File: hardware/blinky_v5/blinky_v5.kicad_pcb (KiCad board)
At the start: 2 copper layers, 130 x 70 mm, 237 parts, among them J1 RJ45, J10 Conn_01x04, J11 Conn_01x08, J12 Conn_01x06, J2 Conn_01x06_Pin, J3 Conn_01x05_Pin, J5 Conn_01x06_Pin, J6 Conn_01x04_Pin, J7 Conn_01x04_Pin, J8 Conn_01x02, J9 Conn_02x10_Odd_Even, Q1 2N7002, Q2 2N7002, Q3 2N7002, Q4 2N7002, Q5 2N7002, Q6 2N7002, Q7 2N7002, Q8 2N7002, U1 ADA4807-1, U10 STM32F405RGTx, U11 AMS1117-3.3, U12 BA50DD0WHFP-TR, U13 M24C02-RMN, U2 SN74LVC1G14DBV, U3 SN74LVC1G14DBV, U4 ADA4807-1, U5 ADA4807-1, U6 TLV3603DCKR, U7 SN74LVC1G14DBV, U8 TLV3603DCKR, U9 L78L05_SOT89, X1 GTXO-14V (2.048MHz), X2 GTXO-14V (2.048MHz), Y1 AOCJY4A-10.000MHZ-SW, Y2 16MHz

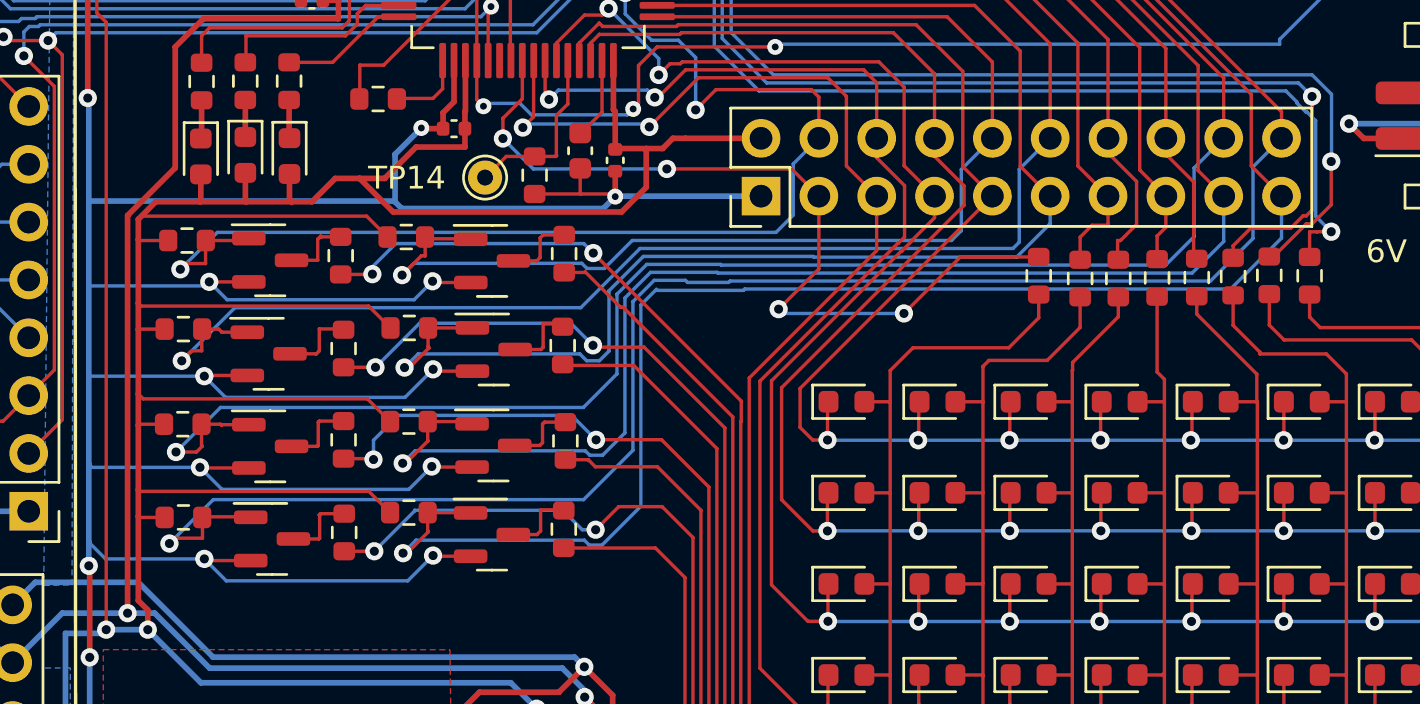
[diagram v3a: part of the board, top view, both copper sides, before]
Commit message: move LED resistors to pull down from pull up
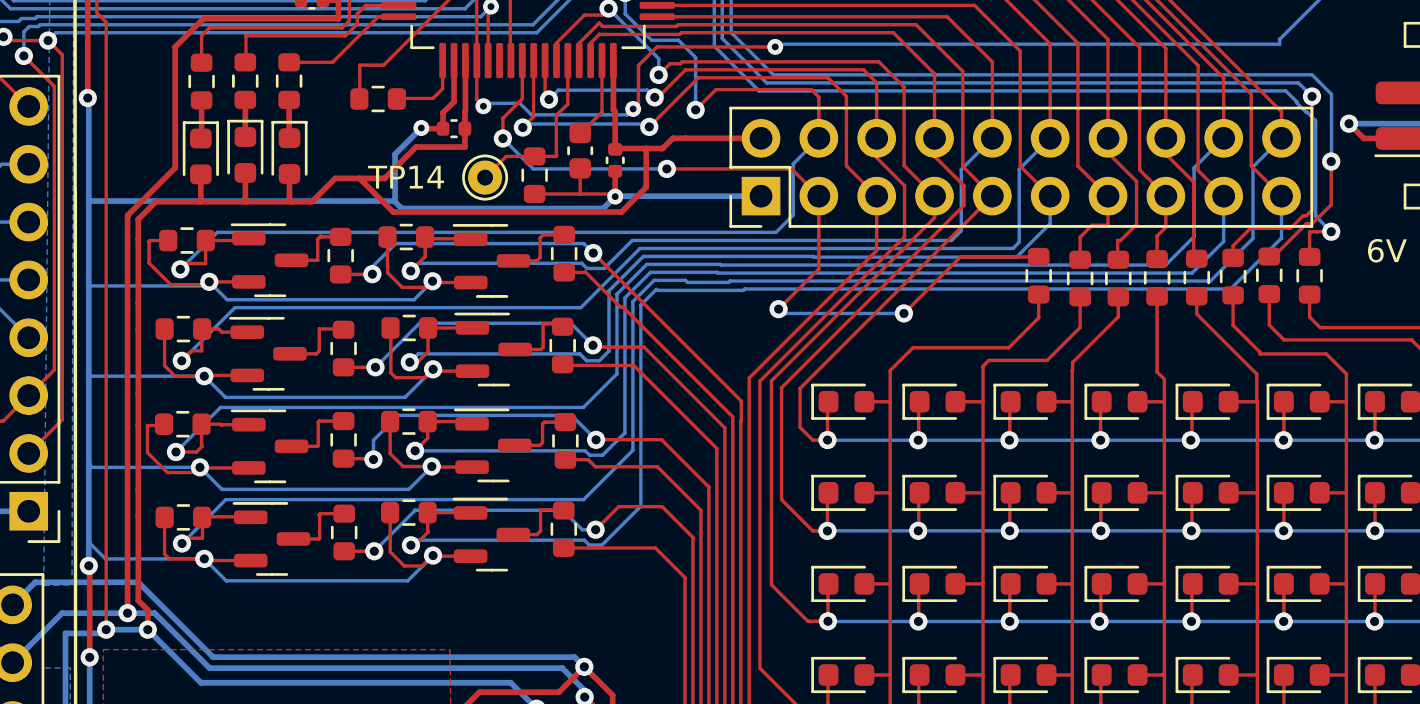
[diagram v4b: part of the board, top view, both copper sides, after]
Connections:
- R33 pad 1: +3.3V -> GND
- R35 pad 1: +3.3V -> GND
- R37 pad 1: +3.3V -> GND
- R39 pad 1: +3.3V -> GND
- R41 pad 1: +3.3V -> GND
- R43 pad 1: +3.3V -> GND
- R45 pad 1: +3.3V -> GND
- R47 pad 1: +3.3V -> GND
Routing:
- net +3.3V: track 468.5 -> 417.8 mm
- net GND: track 1175.8 -> 1207.8 mm
- net /LEDE: track 83.1 -> 81.5 mm
- net /LEDB: track 99.4 -> 98.3 mm
- net /LEDC: track 90.6 -> 89.7 mm
- net /LEDH: track 53.3 -> 52.4 mm
- net /LEDG: track 62.0 -> 61.4 mm

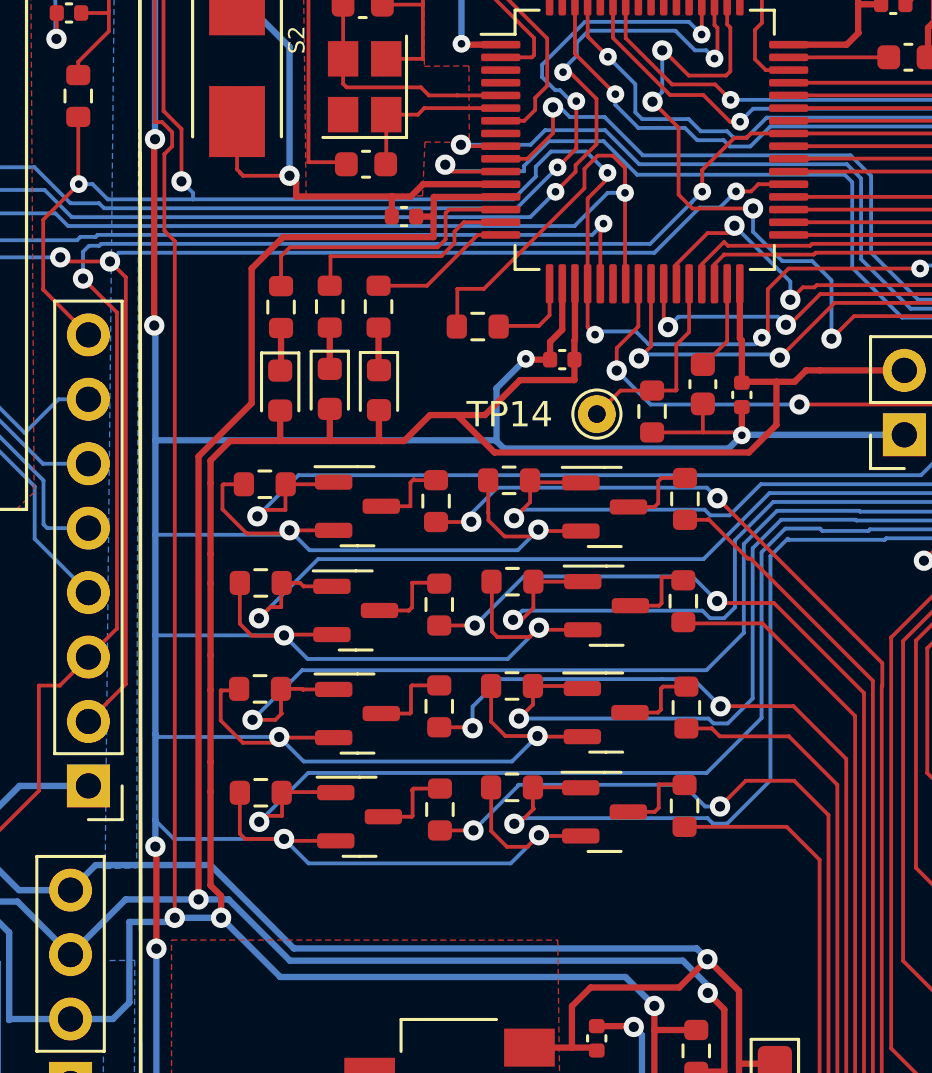
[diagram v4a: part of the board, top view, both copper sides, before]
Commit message: update to have FET drivers for some of status LEDs
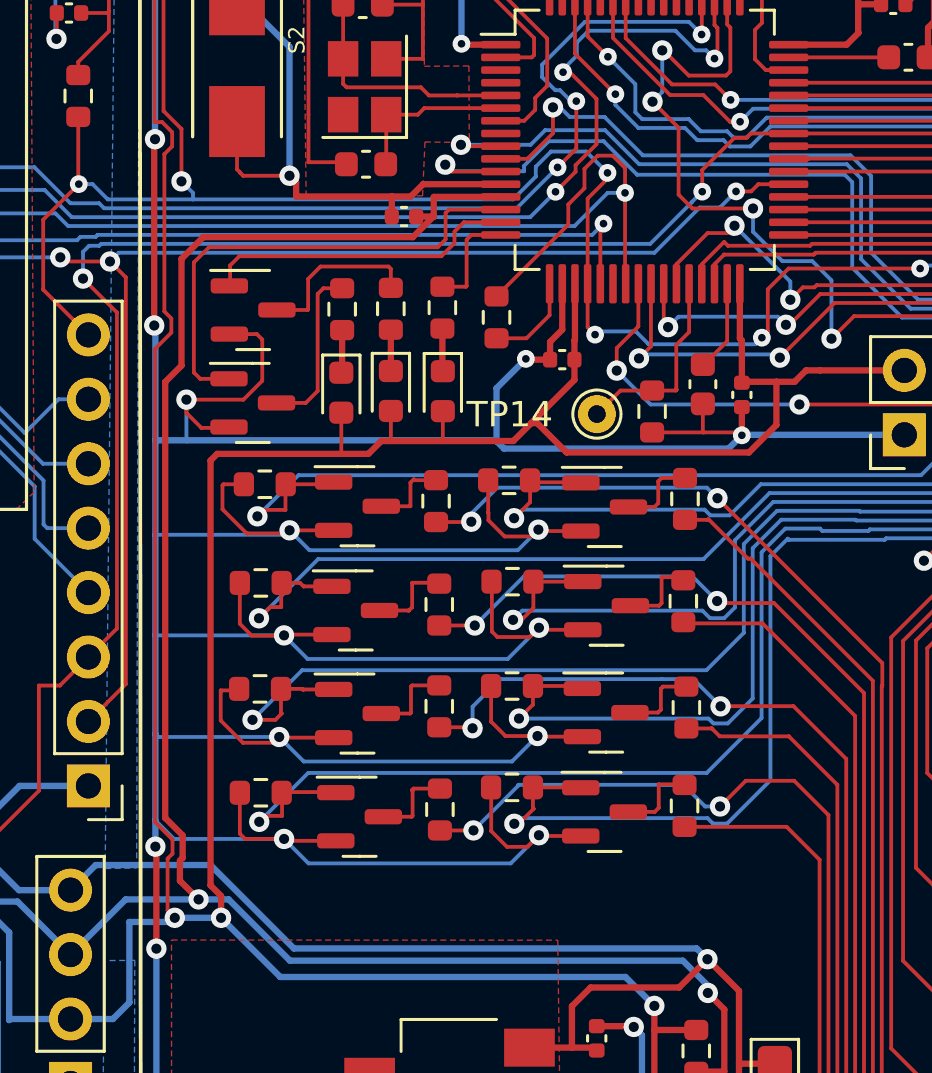
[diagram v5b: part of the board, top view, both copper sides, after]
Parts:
- added Q10: 2N7002, Package_TO_SOT_SMD:SOT-23, F.Cu at (167.6, 81.7)
- added Q9: 2N7002, Package_TO_SOT_SMD:SOT-23, F.Cu at (167.6, 78.0)
- moved D1 2.52 mm to (175.1, 81.2)
- moved R30 2.52 mm to (175.0, 78.0)
- moved D2 2.41 mm to (173.0, 81.2)
- moved D3 2.41 mm to (171.1, 81.3)
- moved R29 2.41 mm to (173.0, 78.0)
- moved R31 2.41 mm to (171.1, 78.0)
- moved R54 0.83 mm to (177.2, 78.3), turned to -90 degrees
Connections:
- R29 pad 2: /LEDM1 -> Net-(Q9-D)
- R31 pad 2: /LEDM3 -> Net-(Q10-D)
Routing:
- net GND: track 1207.8 -> 1218.2 mm, vias 60 -> 61
- net /LEDM3: track 11.2 -> 19.4 mm
- net Net-(Q10-D): track 0.00 -> 6.70 mm
- net Net-(Q9-D): track 0.00 -> 6.69 mm
- net /LEDM1: track 8.71 -> 12.5 mm
- net +3.3VA: track 201.7 -> 204.3 mm
- net SYNC_OUT: track 115.0 -> 112.5 mm
- net +3.3V: track 417.8 -> 415.8 mm
- net /LEDM2: track 5.65 -> 4.21 mm

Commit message: update schematic for new pin out
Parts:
- removed JP5: SolderJumper_2_Bridged, Jumper:SolderJumper-2_P1.3mm_Bridged_RoundedPad1.0x1.5mm
- removed X1: GTXO-14V (2.048MHz), Oscillator:Oscillator_DIP-14
- added J4: Conn_01x04_Pin, Connector_PinHeader_2.54mm:PinHeader_1x04_P2.54mm_Vertical, F.Cu at (235.8, 66.6)
- added R60: 1K0, Resistor_SMD:R_0603_1608Metric, F.Cu at (141.5, 125.4)
- added R61: 1K0, Resistor_SMD:R_0603_1608Metric, F.Cu at (149.4, 125.9)
- added R62: 1K0, Resistor_SMD:R_0603_1608Metric, F.Cu at (172.3, 134.5)
- added R63: 1K0, Resistor_SMD:R_0603_1608Metric, F.Cu at (161.1, 139.2)
- added R64: 1K0, Resistor_SMD:R_0603_1608Metric, F.Cu at (190.6, 136.1)
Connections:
- J11 pad 3: EXT_CLK_IN -> /CLK
- J12 pad 3: /SWDTRC -> GND
- TP10 pad 1: EXT_CLK_IN -> AUX_CLK
- TP3 pad 1: SYNC_IN -> Net-(R63-Pad2)
- TP8 pad 1: GPS_PPS -> Net-(U8-OUT)
- U10 pad 14: /LEDM3 -> AUX_CLK
- U10 pad 15: /LEDM1 -> AUX_GPS_PPS
- U10 pad 16: /LEDM2 -> /AUX_SYNC_MON
- U10 pad 17: /SYNC_MON -> /LEDM3
- U10 pad 21: SYNC_IN -> /AUD_OUT
- U10 pad 22: unconnected-(U10-PA6-Pad22) -> /COL1
- U10 pad 23: SYNC_OUT -> /COL2
- U10 pad 29: /COL2 -> GPS_PPS
- U10 pad 3: unconnected-(U10-PC14-Pad3) -> /LEDM1
- U10 pad 30: /COL1 -> /SYNC_MON
- U10 pad 37: GPS_PPS -> SYNC_IN2
- U10 pad 4: unconnected-(U10-PC15-Pad4) -> /LEDM2
- U10 pad 41: EXT_CLK_IN -> SYNC_OUT
- U10 pad 50: /LEDA -> /CLK
- U10 pad 53: /DB4 -> /LEDA
- U10 pad 55: /SWDTRC -> SYNC_IN
- U10 pad 8: unconnected-(U10-PC0-Pad8) -> /AUD_IN
- U3 pad 4: SYNC_IN -> Net-(R63-Pad2)
- U7 pad 4: Net-(JP5-A) -> AUX_CLK
- U8 pad 1: GPS_PPS -> Net-(U8-OUT)
- X2 pad 8: EXT_CLK_IN -> /CLK
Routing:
- net (no net): track 0.00 -> 152.3 mm
- net EXT_CLK_IN: track 125.3 -> 0.00 mm, vias 6 -> 0
- net GND: track 1218.2 -> 1185.7 mm, vias 61 -> 60
- net /SWDTRC: track 27.0 -> 0.00 mm, vias 2 -> 0
- net /OCXO_OUT: track 69.9 -> 63.3 mm
- net /Vadj: track 56.0 -> 49.5 mm
- net Net-(JP5-A): track 3.31 -> 0.00 mm
- net AUX_CLK: track 0.00 -> 3.31 mm
- net +3.3VA: track 204.3 -> 205.2 mm
- net SYNC_IN: vias 4 -> 6
- net /CLK: vias 0 -> 6

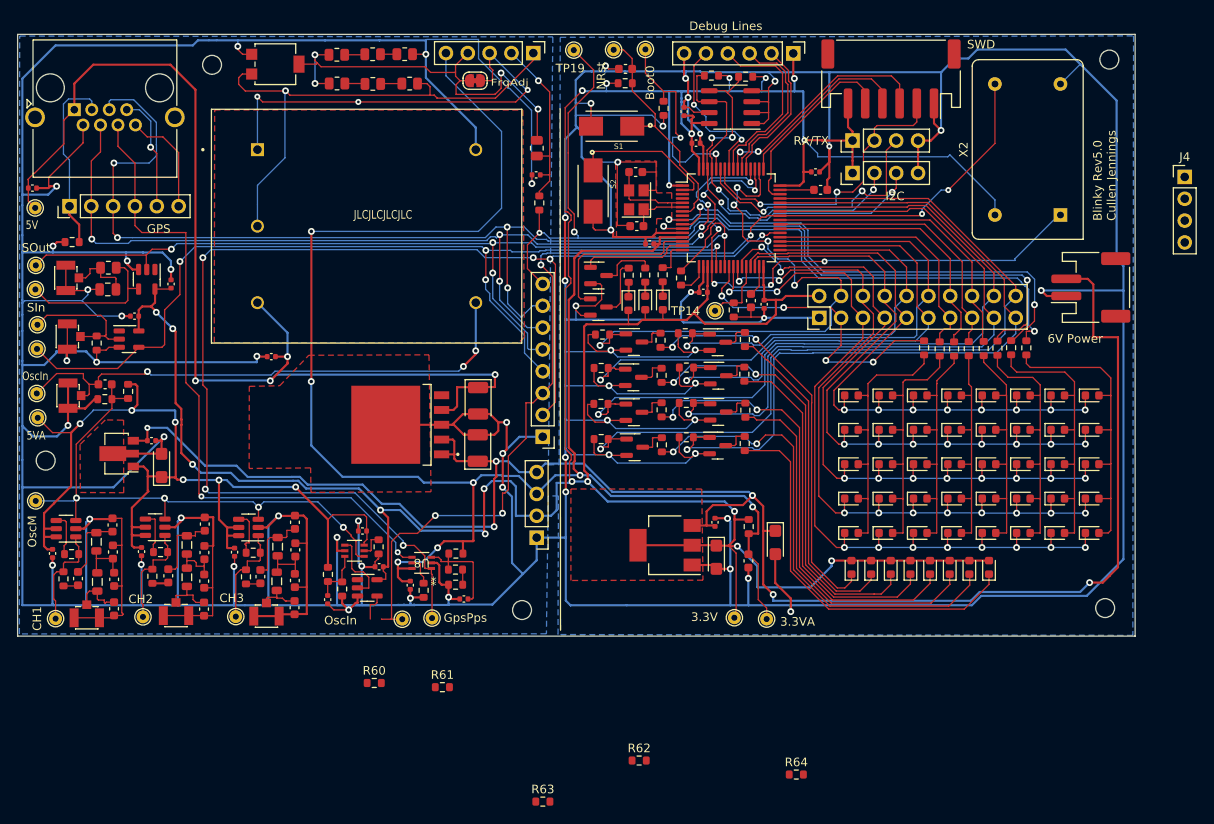
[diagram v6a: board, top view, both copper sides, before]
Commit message: update scehmatic with new pin out
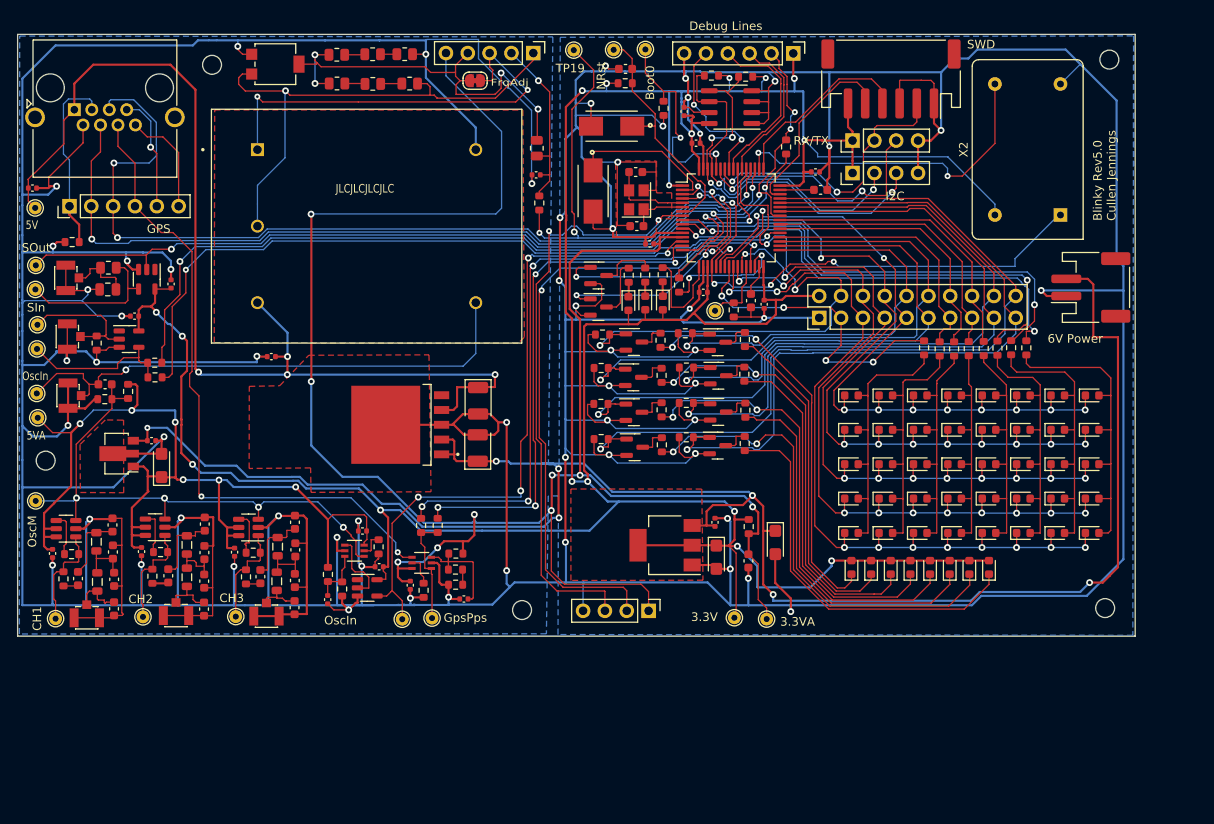
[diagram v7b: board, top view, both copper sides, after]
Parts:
- removed J10: Conn_01x04, Connector_PinHeader_2.54mm:PinHeader_1x04_P2.54mm_Vertical
- removed J11: Conn_01x08, Connector_PinHeader_2.54mm:PinHeader_1x08_P2.54mm_Vertical
- moved R64 87.7 mm to (116.0, 89.9), turned to 180 degrees
- moved J4 80.2 mm to (173.4, 117.1), turned to -90 degrees
- moved R62 73.4 mm to (189.4, 63.1), turned to -90 degrees
- moved R63 68.2 mm to (115.9, 88.2), turned to 180 degrees
- moved R60 19.1 mm to (146.9, 107.1), turned to -90 degrees
- moved R61 18.8 mm to (148.9, 107.1), turned to 90 degrees
- moved R54 0.85 mm to (176.9, 79.2)
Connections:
- J5 pad 2: /DB4 -> SYNC_OUT
- U10 pad 17: /LEDM3 -> /LEDM2
- U10 pad 3: /LEDM1 -> /LEDM3
- U10 pad 4: /LEDM2 -> /LEDM1
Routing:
- net (no net): track 152.3 -> 0.00 mm
- net SYNC_IN2: track 0.00 -> 86.2 mm, vias 0 -> 2
- net GPS_PPS: track 152.6 -> 71.2 mm, vias 6 -> 4
- net AUX_CLK: track 3.31 -> 77.2 mm, vias 0 -> 4
- net /AUD_OUT: track 0.00 -> 73.5 mm, vias 0 -> 2
- net /AUD_IN: track 0.00 -> 69.4 mm, vias 0 -> 2
- net AUX_GPS_PPS: track 0.00 -> 59.7 mm, vias 0 -> 4
- net /CLK: track 0.00 -> 39.6 mm, vias 6 -> 2
- net +3.3VA: track 205.2 -> 229.6 mm, vias 7 -> 9
- net /AUX_SYNC_MON: track 0.00 -> 22.2 mm, vias 0 -> 2
- net SYNC_IN: track 110.4 -> 88.7 mm, vias 6 -> 2
- net /LEDM1: track 12.5 -> 32.9 mm, vias 0 -> 4
- net /GPS_RX1: track 116.3 -> 98.1 mm, vias 6 -> 2
- net Net-(R63-Pad2): track 0.00 -> 18.1 mm
- net /GPS_TX1: track 123.7 -> 105.7 mm, vias 7 -> 3
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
